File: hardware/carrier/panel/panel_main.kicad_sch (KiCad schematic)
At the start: 22 parts, among them J1 GDEY029T94 FPC, J2 CARRIER, Q5 AO3400A

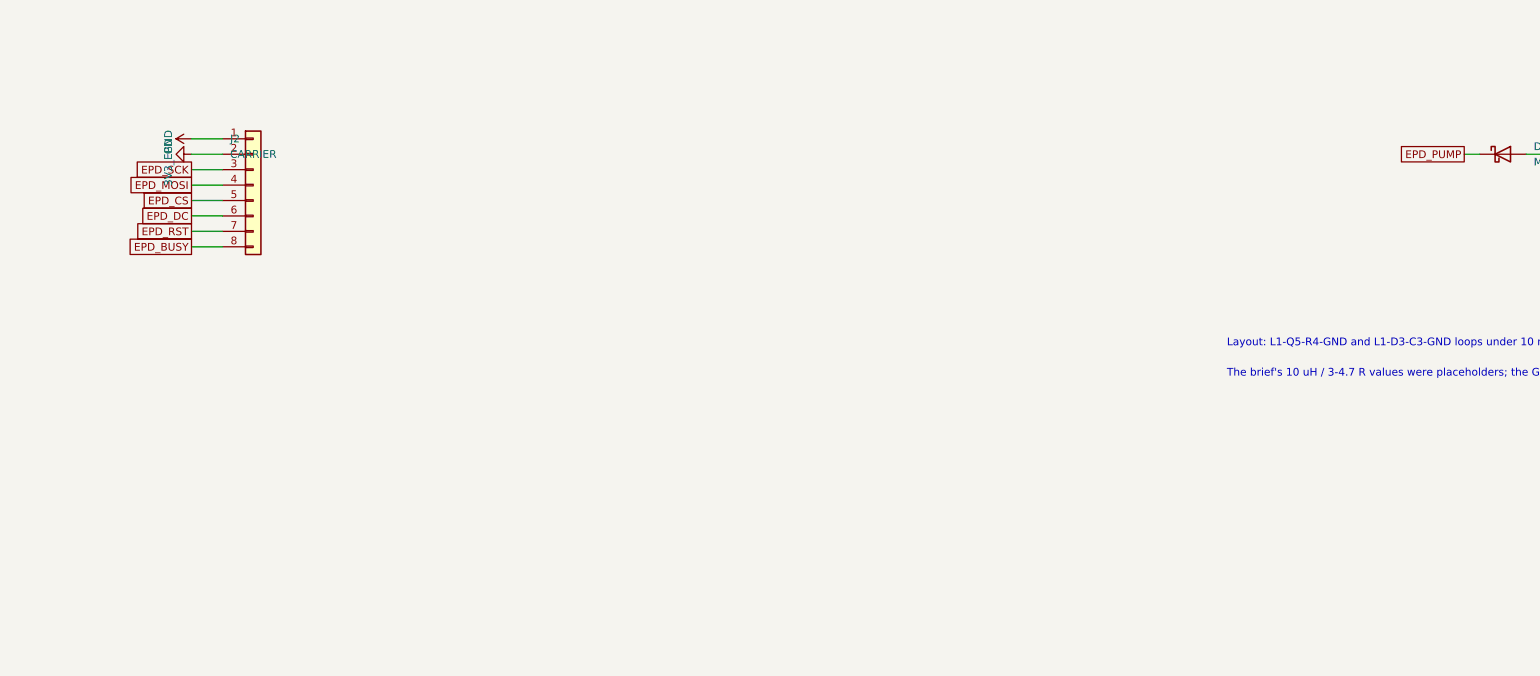
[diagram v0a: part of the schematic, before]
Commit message: hardware/carrier: front light is the GDEY029T94-FL03 (6-pin flex -> FH34SRJ-6S on the panel board, anode/cathode over a 10-way SH cable, 33R 1206 + Q4 PWM drive replaces the NSI45020), front-light button SW2 on IO4 (FL_BTN), low-profile pass (FH34SRJ 1.0 mm ZIFs, 2 x 100uF 0805 instead of the 2.5 mm 1210, part-height table), sleep-current audit (Q1 gate pull-up 100k -> 2.2M: 38 -> 1.9 uA; SN74LVC2G126 moved to the bus-powered BRG_VDD rail: 0 on battery; table in the README), TPS62840 has no fixed-3.3 V variant (README). Custom FH34SRJ footprints from the Hirose catalog; LCSC numbers via the JLCPCB parts API. Both boards re-placed and re-routed: 0 unconnected, 0 clearance/courtyard errors, silk notes only; ERC 0/0; exports refreshed (owner, 17 Oct 2026)
Co-Authored-By: Claude Fable 5.1 <noreply@anthropic.com>
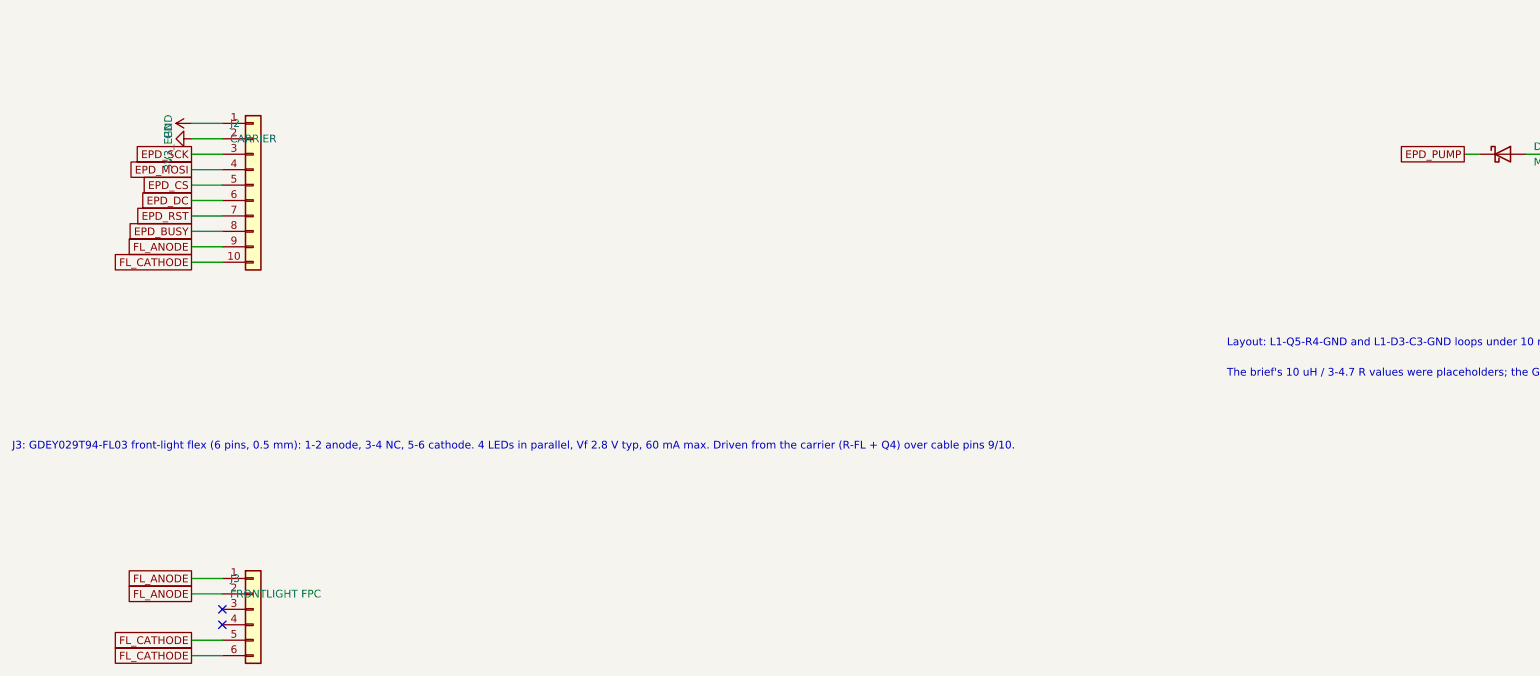
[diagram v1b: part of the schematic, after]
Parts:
- added J3: FRONTLIGHT FPC, pager-carrier:Hirose_FH34SRJ-6S-0.5SH_1x06-1MP_P0.50mm_Horizontal, symbol Connector_Generic:Conn_01x06
- J1: footprint Connector_FFC-FPC:Hirose_FH12-24S-0.5SH_1x24-1MP_P0.50mm_Horizontal -> pager-carrier:Hirose_FH34SRJ-24S-0.5SH_1x24-1MP_P0.50mm_Horizontal; LCSC C202112 -> C324726; MPN FH12-24S-0.5SH(55) -> FH34SRJ-24S-0.5SH(50); Note bottom contact; FPC folded 180 deg under the glass -> 1.0 mm high, top+bottom contact; FPC folded 180 deg under t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
- J2: footprint Connector_JST:JST_SH_SM08B-SRSS-TB_1x08-1MP_P1.00mm_Horizontal -> Connector_JST:JST_SH_SM10B-SRSS-TB_1x10-1MP_P1.00mm_Horizontal; symbol Connector_Generic:Conn_01x08 -> Connector_Generic:Conn_01x10; LCSC C160407 -> C160409; MPN SM08B-SRSS-TB -> SM10B-SRSS-TB; Note to carrier J3, 1:1 8-way SH cable -> to carrier J3, 1:1 10-way SH cable
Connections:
- new net FL_ANODE: J2.9 (Pin_9), J3.1 (Pin_1), J3.2 (Pin_2)
- new net FL_CATHODE: J2.10 (Pin_10), J3.5 (Pin_5), J3.6 (Pin_6)
- no-connect marks 5 -> 7
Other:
- note added: "J3: GDEY029T94-FL03 front-light flex (6 pins, 0.5 mm): 1-2 anode, 3-4 NC, 5-6 cathode. 4 LEDs in parallel, Vf 2.8 V typ, 60 mA max. Driven from the carrier (R-FL + Q4) over cable pins 9/10."
